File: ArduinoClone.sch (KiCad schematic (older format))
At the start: 9 parts

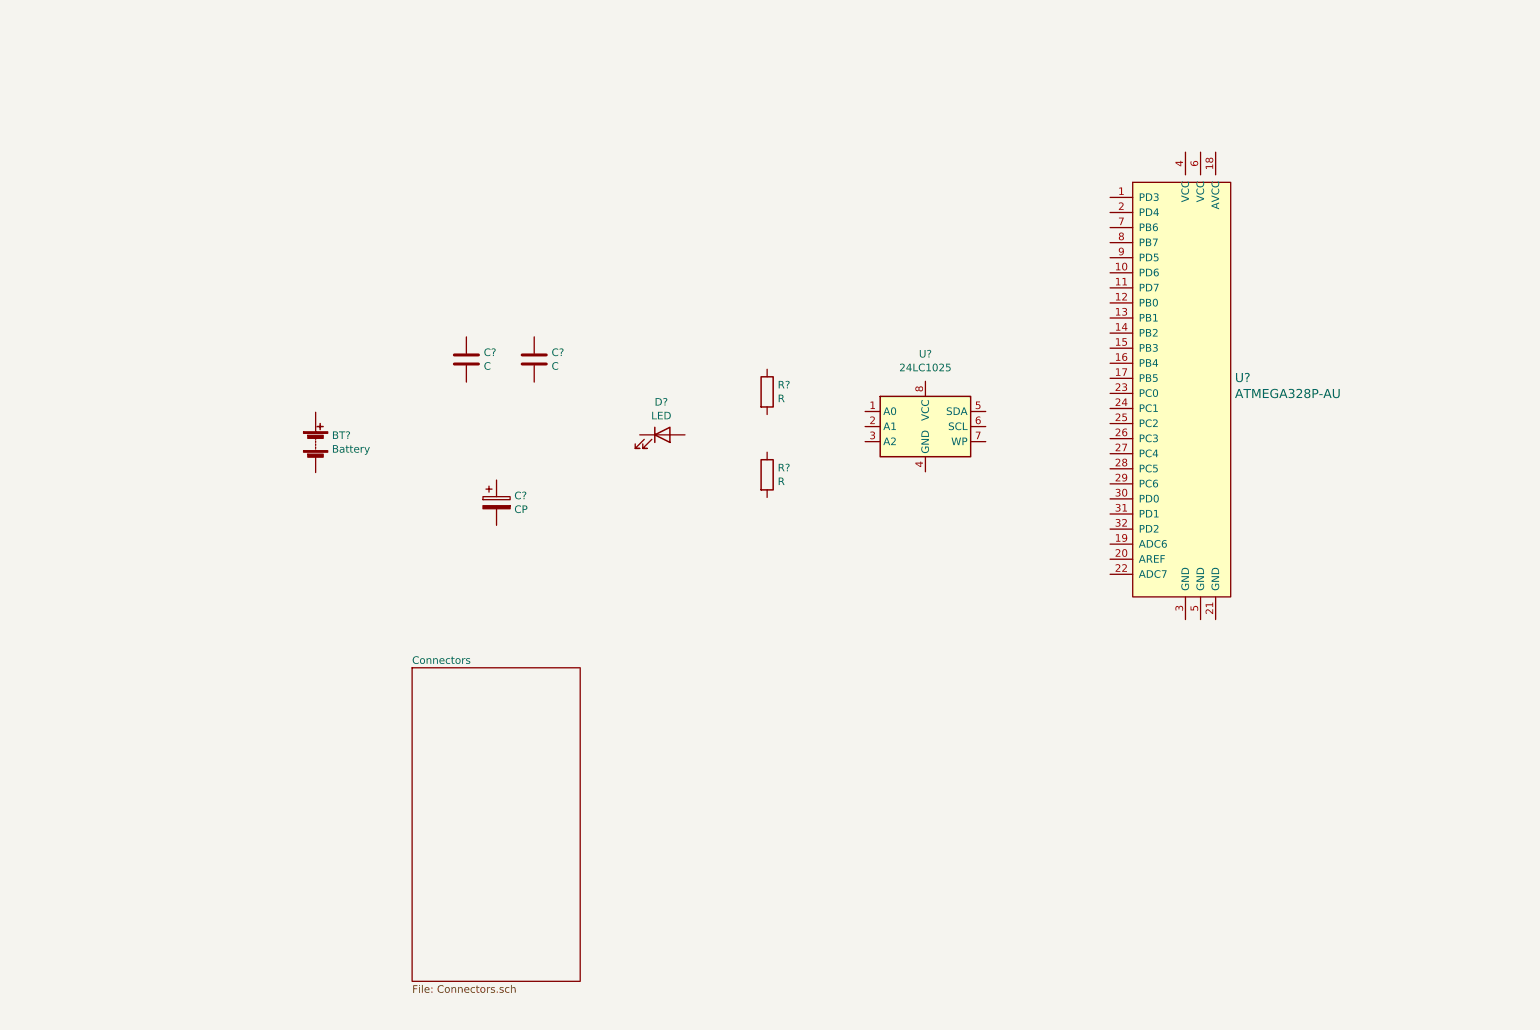
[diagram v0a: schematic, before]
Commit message: footprints associated to symbols
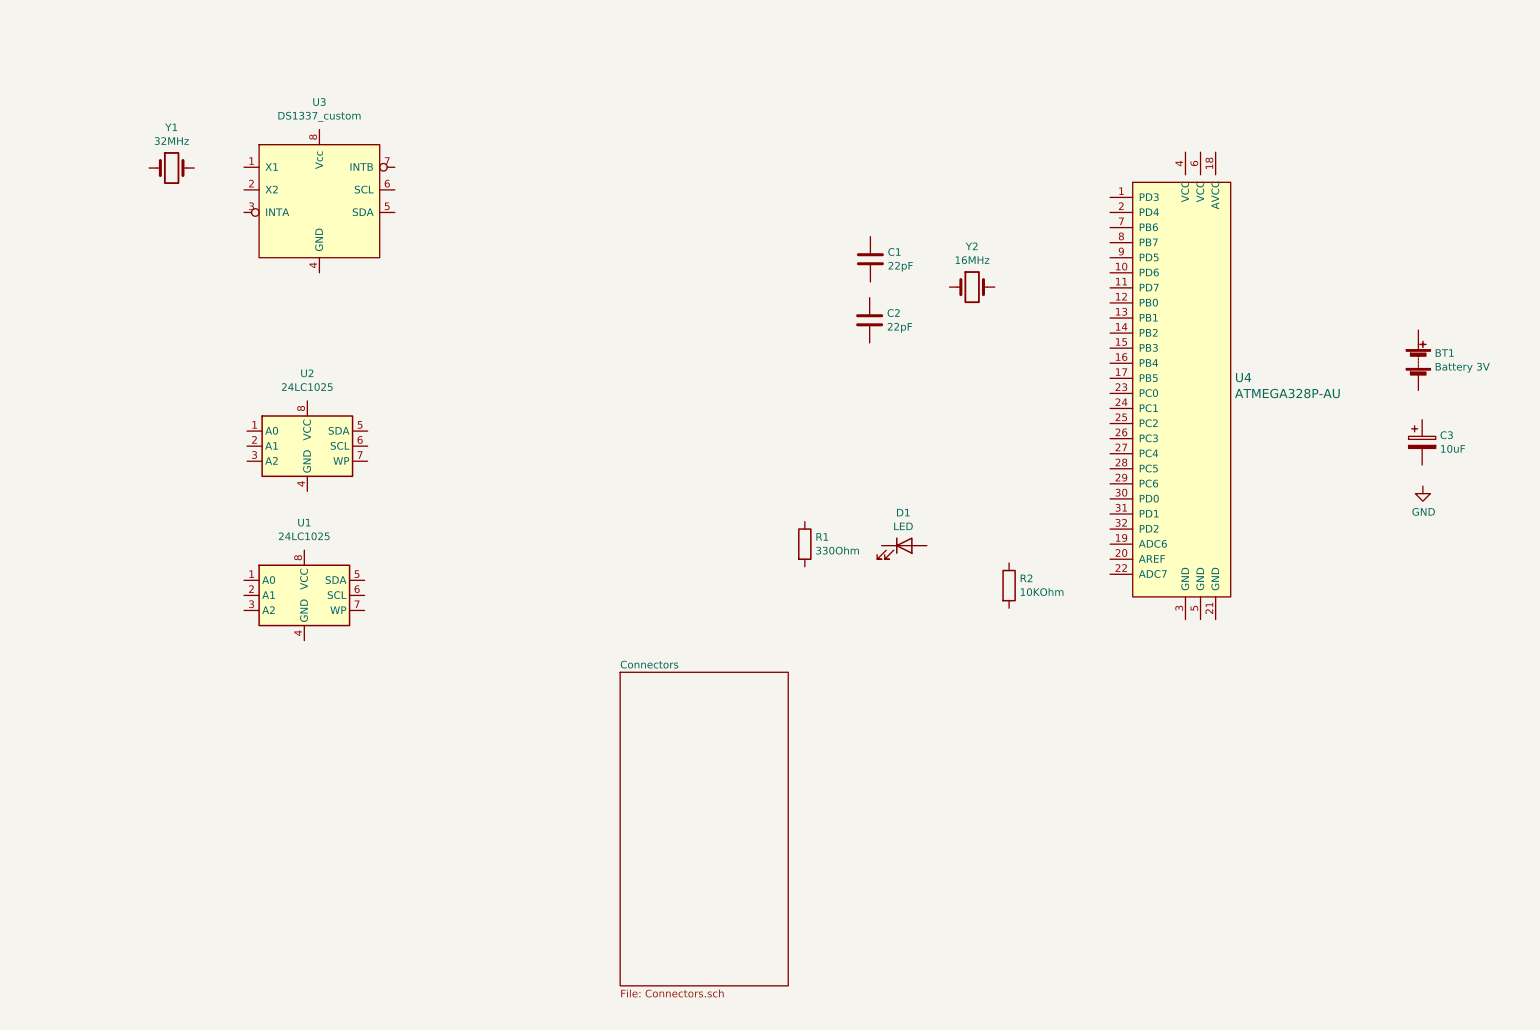
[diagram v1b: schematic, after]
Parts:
- added U1: 24LC1025, Package_SO:SOIJ-8_5.3x5.3mm_P1.27mm, symbol Memory_EEPROM:24LC1025
- added U3: DS1337_custom, Package_SO:SO-8_5.3x6.2mm_P1.27mm, symbol ArduinoClone:DS1337_custom
- added Y1: 32MHz, Crystal:Crystal_SMD_MicroCrystal_CC7V-T1A-2Pin_3.2x1.5mm_HandSoldering, symbol Device:Crystal
- added Y2: 16MHz, Crystal:Crystal_SMD_5032-2Pin_5.0x3.2mm, symbol Device:Crystal
- BT1: renamed from BT?; value Battery -> Battery 3V; footprint (none) -> Connector_PinHeader_2.54mm:PinHeader_1x02_P2.54mm_Vertical
- C1, C2: renamed from C?; value C -> 22pF; footprint (none) -> Capacitor_SMD:C_0805_2012Metric_Pad1.15x1.40mm_HandSolder
- C3: renamed from C?; value CP -> 10uF; footprint (none) -> Capacitor_SMD:C_0805_2012Metric_Pad1.15x1.40mm_HandSolder
- D1: renamed from D?; footprint (none) -> LED_SMD:LED_0805_2012Metric_Pad1.15x1.40mm_HandSolder
- R1: renamed from R?; value R -> 330Ohm; footprint (none) -> Resistor_SMD:R_0805_2012Metric_Pad1.15x1.40mm_HandSolder
- R2: renamed from R?; value R -> 10KOhm; footprint (none) -> Resistor_SMD:R_0805_2012Metric_Pad1.15x1.40mm_HandSolder
- U2: renamed from U?; footprint (none) -> Package_SO:SOIJ-8_5.3x5.3mm_P1.27mm
- gave numbers to parts that had none: 1
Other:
- moved on the sheet: BT1, C1, C2, C3, D1, R1, R2, U2
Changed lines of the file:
@@
 $EndDescr
 $Comp
-L Device:Battery BT?
+L Device:Battery BT1
 U 1 1 5FC29141
-P 3050 3750
-F 0 "BT?" H 3158 3796 50  0000 L CNN
-F 1 "Battery" H 3158 3705 50  0000 L CNN
-F 2 "" V 3050 3810 50  0001 C CNN
-F 3 "~" V 3050 3810 50  0001 C CNN
-	1    3050 3750
+P 10365 3205
+F 0 "BT1" H 10473 3251 50  0000 L CNN
+F 1 "Battery 3V" H 10473 3160 50  0000 L CNN
+F 2 "Connector_PinHeader_2.54mm:PinHeader_1x02_P2.54mm_Vertical" V 10365 3265 50  0001 C CNN
+F 3 "~" V 10365 3265 50  0001 C CNN
+	1    10365 3205
 	1    0    0    -1
 $EndComp
 $Comp
-L Device:C C?
+L Device:C C1
 U 1 1 5FC29726
-P 4050 3200
-F 0 "C?" H 4165 3246 50  0000 L CNN
-F 1 "C" H 4165 3155 50  0000 L CNN
-F 2 "" H 4088 3050 50  0001 C CNN
-F 3 "~" H 4050 3200 50  0001 C CNN
-	1    4050 3200
+P 6730 2535
+F 0 "C1" H 6845 2581 50  0000 L CNN
+F 1 "22pF" H 6845 2490 50  0000 L CNN
+F 2 "Capacitor_SMD:C_0805_2012Metric_Pad1.15x1.40mm_HandSolder" H 6768 2385 50  0001 C CNN
+F 3 "~" H 6730 2535 50  0001 C CNN
+	1    6730 2535
 	1    0    0    -1
 $EndComp
 $Comp
-L Device:C C?
+L Device:C C2
 U 1 1 5FC299AA
-P 4500 3200
-F 0 "C?" H 4615 3246 50  0000 L CNN
-F 1 "C" H 4615 3155 50  0000 L CNN
-F 2 "" H 4538 3050 50  0001 C CNN
-F 3 "~" H 4500 3200 50  0001 C CNN
-	1    4500 3200
+P 6725 2940
+F 0 "C2" H 6840 2986 50  0000 L CNN
+F 1 "22pF" H 6840 2895 50  0000 L CNN
+F 2 "Capacitor_SMD:C_0805_2012Metric_Pad1.15x1.40mm_HandSolder" H 6763 2790 50  0001 C CNN
+F 3 "~" H 6725 2940 50  0001 C CNN
+	1    6725 2940
 	1    0    0    -1
 $EndComp
 $Comp
-L Device:CP C?
+L Device:CP C3
 U 1 1 5FC2A1F5
-P 4250 4150
-F 0 "C?" H 4368 4196 50  0000 L CNN
-F 1 "CP" H 4368 4105 50  0000 L CNN
-F 2 "" H 4288 4000 50  0001 C CNN
-F 3 "~" H 4250 4150 50  0001 C CNN
-	1    4250 4150
+P 10390 3750
+F 0 "C3" H 10508 3796 50  0000 L CNN
+F 1 "10uF" H 10508 3705 50  0000 L CNN
+F 2 "Capacitor_SMD:C_0805_2012Metric_Pad1.15x1.40mm_HandSolder" H 10428 3600 50  0001 C CNN
+F 3 "~" H 10390 3750 50  0001 C CNN
+	1    10390 3750
 	1    0    0    -1
 $EndComp
 $Comp
-L Device:LED D?
+L Device:LED D1
 U 1 1 5FC2A967
-P 5350 3700
-F 0 "D?" H 5343 3917 50  0000 C CNN
-F 1 "LED" H 5343 3826 50  0000 C CNN
-F 2 "" H 5350 3700 50  0001 C CNN
-F 3 "~" H 5350 3700 50  0001 C CNN
-	1    5350 3700
+P 6955 4435
+F 0 "D1" H 6948 4652 50  0000 C CNN
+F 1 "LED" H 6948 4561 50  0000 C CNN
+F 2 "LED_SMD:LED_0805_2012Metric_Pad1.15x1.40mm_HandSolder" H 6955 4435 50  0001 C CNN
+F 3 "~" H 6955 4435 50  0001 C CNN
+	1    6955 4435
 	1    0    0    -1
 $EndComp
 $Comp
-L Device:R R?
+L Device:R R1
 U 1 1 5FC2AE6E
-P 6045 3415
-F 0 "R?" H 6115 3461 50  0000 L CNN
-F 1 "R" H 6115 3370 50  0000 L CNN
-F 2 "" V 5975 3415 50  0001 C CNN
-F 3 "~" H 6045 3415 50  0001 C CNN
-	1    6045 3415
+P 6295 4425
+F 0 "R1" H 6365 4471 50  0000 L CNN
+F 1 "330Ohm" H 6365 4380 50  0000 L CNN
+F 2 "Resistor_SMD:R_0805_2012Metric_Pad1.15x1.40mm_HandSolder" V 6225 4425 50  0001 C CNN
+F 3 "~" H 6295 4425 50  0001 C CNN
+	1    6295 4425
 	1    0    0    -1
 $EndComp
 $Comp
-L Device:R R?
+L Device:R R2
 U 1 1 5FC2B18E
-P 6045 3965
-F 0 "R?" H 6115 4011 50  0000 L CNN
-F 1 "R" H 6115 3920 50  0000 L CNN
-F 2 "" V 5975 3965 50  0001 C CNN
-F 3 "~" H 6045 3965 50  0001 C CNN
-	1    6045 3965
+P 7650 4700
+F 0 "R2" H 7720 4746 50  0000 L CNN
+F 1 "10KOhm" H 7720 4655 50  0000 L CNN
+F 2 "Resistor_SMD:R_0805_2012Metric_Pad1.15x1.40mm_HandSolder" V 7580 4700 50  0001 C CNN
+F 3 "~" H 7650 4700 50  0001 C CNN
+	1    7650 4700
 	1    0    0    -1
 $EndComp
 $Comp
-L Memory_EEPROM:24LC1025 U?
+L Memory_EEPROM:24LC1025 U2
 U 1 1 5FC2B9FB
-P 7095 3645
-F 0 "U?" H 7095 4126 50  0000 C CNN
-F 1 "24LC1025" H 7095 4035 50  0000 C CNN
-F 2 "" H 7095 3645 50  0001 C CNN
-F 3 "http://ww1.microchip.com/downloads/en/DeviceDoc/21941B.pdf" H 7095 3645 50  0001 C CNN
-	1    7095 3645
+P 2995 3775
+F 0 "U2" H 2995 4256 50  0000 C CNN
+F 1 "24LC1025" H 2995 4165 50  0000 C CNN
+F 2 "Package_SO:SOIJ-8_5.3x5.3mm_P1.27mm" H 2995 3775 50  0001 C CNN
+F 3 "http://ww1.microchip.com/downloads/en/DeviceDoc/21941B.pdf" H 2995 3775 50  0001 C CNN
+	1    2995 3775
 	1    0    0    -1
 $EndComp
 $Comp
-L dk_Embedded-Microcontrollers:ATMEGA328P-AU U?
+L dk_Embedded-Microcontrollers:ATMEGA328P-AU U4
 U 1 1 5FC2CA71
 P 8820 3425
-F 0 "U?" H 9148 3528 60  0000 L CNN
+F 0 "U4" H 9148 3528 60  0000 L CNN
 F 1 "ATMEGA328P-AU" H 9148 3422 60  0000 L CNN
 F 2 "digikey-footprints:TQFP-32_7x7mm" H 9020 3625 60  0001 L CNN
@@
 $EndComp
 $Sheet
-S 3690 5245 1115 2080
+S 5070 5275 1115 2080
 U 5FC2F143
 F0 "Connectors" 50
 F1 "Connectors.sch" 50
 $EndSheet
+$Comp
+L ArduinoClone:DS1337_custom U3
+U 1 1 5FC34461
+P 3075 1575
+F 0 "U3" H 3075 1656 50  0000 C CNN
+F 1 "DS1337_custom" H 3075 1565 50  0000 C CNN
+F 2 "Package_SO:SO-8_5.3x6.2mm_P1.27mm" H 3075 1575 50  0001 C CNN
+F 3 "" H 3075 1575 50  0001 C CNN
+	1    3075 1575
+	1    0    0    -1
+$EndComp
+$Comp
+L Device:Crystal Y1
+U 1 1 5FC35372
+P 2095 1930
+F 0 "Y1" H 2095 2198 50  0000 C CNN
+F 1 "32MHz" H 2095 2107 50  0000 C CNN
+F 2 "Crystal:Crystal_SMD_MicroCrystal_CC7V-T1A-2Pin_3.2x1.5mm_HandSoldering" H 2095 1930 50  0001 C CNN
+F 3 "~" H 2095 1930 50  0001 C CNN
+	1    2095 1930
+	1    0    0    -1
+$EndComp
+$Comp
+L Device:Crystal Y2
+U 1 1 5FC35EBB
+P 7405 2720
+F 0 "Y2" H 7405 2988 50  0000 C CNN
+F 1 "16MHz" H 7405 2897 50  0000 C CNN
+F 2 "Crystal:Crystal_SMD_5032-2Pin_5.0x3.2mm" H 7405 2720 50  0001 C CNN
+F 3 "~" H 7405 2720 50  0001 C CNN
+	1    7405 2720
+	1    0    0    -1
+$EndComp
+$Comp
+L Memory_EEPROM:24LC1025 U1
+U 1 1 5FC3C754
+P 2975 4765
+F 0 "U1" H 2975 5246 50  0000 C CNN
+F 1 "24LC1025" H 2975 5155 50  0000 C CNN
+F 2 "Package_SO:SOIJ-8_5.3x5.3mm_P1.27mm" H 2975 4765 50  0001 C CNN
+F 3 "http://ww1.microchip.com/downloads/en/DeviceDoc/21941B.pdf" H 2975 4765 50  0001 C CNN
+	1    2975 4765
+	1    0    0    -1
+$EndComp
+$Comp
+L power:GND #PWR01
+U 1 1 5FC3EF92
+P 10395 4040
+F 0 "#PWR01" H 10395 3790 50  0001 C CNN
+F 1 "GND" H 10400 3867 50  0000 C CNN
+F 2 "" H 10395 4040 50  0001 C CNN
+F 3 "" H 10395 4040 50  0001 C CNN
+	1    10395 4040
+	1    0    0    -1
+$EndComp
 $EndSCHEMATC

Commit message: finished schematics with comments
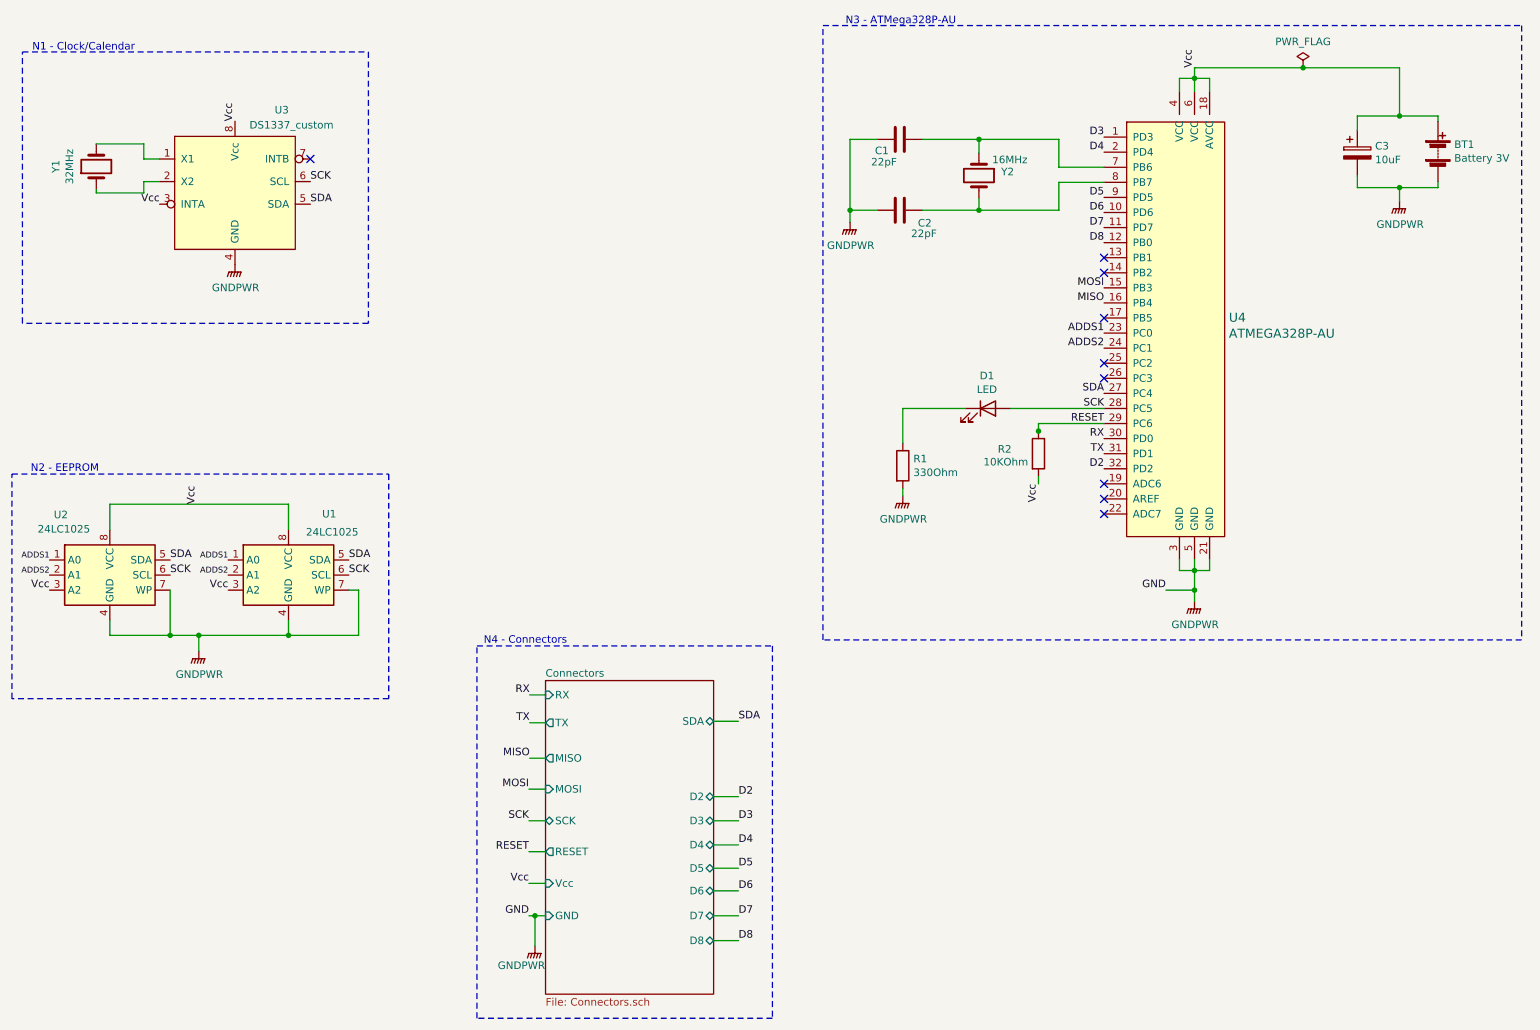
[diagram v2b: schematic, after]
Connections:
- net Vcc: now reaches BT1.1 (+)
- net Vcc: now also C3.1, R2.2, U1.3 (A2), U1.8 (VCC), U2.3 (A2), U2.8 (VCC), U3.3 (INTA), U3.8 (Vcc), U4.18 (AVCC), U4.4 (VCC), U4.6 (VCC)
- net GNDPWR: now reaches BT1.2 (-)
- net GNDPWR: now also C1.2, C2.2, C3.2, R1.2, U1.4 (GND), U1.7 (WP), U2.4 (GND), U2.7 (WP), U3.4 (GND), U4.21 (GND), U4.3 (GND), U4.5 (GND)
- net at C1.1: now also U4.7 (PB6), Y2.1
- net at C2.1: now also U4.8 (PB7), Y2.2
- net at D1.1 (K): now also R1.1
- net SCK: now reaches D1.2 (A)
- net SCK: now also U1.6 (SCL), U2.6 (SCL), U3.6 (SCL), U4.28 (PC5)
- net RESET: now reaches R2.1
- net RESET: now also U4.29 (PC6)
- net ADDS1: now reaches U2.1 (A0)
- net ADDS1: now also U1.1 (A0), U4.23 (PC0)
- net ADDS2: now reaches U2.2 (A1)
- net ADDS2: now also U1.2 (A1), U4.24 (PC1)
- net SDA: now reaches U2.5 (SDA)
- net SDA: now also U1.5 (SDA), U3.5 (SDA), U4.27 (PC4)
- net D3: now reaches U4.1 (PD3)
- net D6: now reaches U4.10 (PD6)
- net D7: now reaches U4.11 (PD7)
- net D8: now reaches U4.12 (PB0)
- net MOSI: now reaches U4.15 (PB3)
- net MISO: now reaches U4.16 (PB4)
- net D4: now reaches U4.2 (PD4)
- net RX: now reaches U4.30 (PD0)
- net TX: now reaches U4.31 (PD1)
- net D2: now reaches U4.32 (PD2)
- net D5: now reaches U4.9 (PD5)
- net at U3.1 (X1): now also Y1.2
- net at U3.2 (X2): now also Y1.1
- no-connect marks 0 -> 9
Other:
- note added: "N1 - Clock/Calendar"
- note added: "N2 - EEPROM"
- note added: "N3 - ATMega328P-AU"
- note added: "N4 - Connectors"
- moved on the sheet: BT1, C1, C2, C3, D1, R1, R2, U1, U2, U3, U4, Y1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
